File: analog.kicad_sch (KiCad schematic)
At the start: 18 parts, among them Q1 S8550, U2 HX711

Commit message: rough blocking out the pcb
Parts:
- removed C9: 100nF, Capacitor_SMD:C_0603_1608Metric, symbol karl-marel-atomics:KC0603_100nF
- removed JP2: Jumper_2_Open, TestPoint:TestPoint_2Pads_Pitch2.54mm_Drill0.8mm, symbol Jumper:Jumper_2_Open
- removed R11, R12: 100R, Resistor_SMD:R_0603_1608Metric, symbol karl-marel-atomics:KR0603_100R
- added C9: 33pF, Capacitor_SMD:C_0603_1608Metric, symbol karl-marel-atomics:KC0603_33pF
- added R11: 10k, Resistor_SMD:R_0603_1608Metric, symbol karl-marel-atomics:KR0603_10k
- added R12: 0R, Resistor_SMD:R_0603_1608Metric, symbol karl-marel-atomics:KR0603_0R
- added TP1: TestPoint, TestPoint:TestPoint_THTPad_1.5x1.5mm_Drill0.7mm, symbol Connector:TestPoint
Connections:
- net EXC+: now also TP1.1
- net GNDA: now also C3.2, C4.2, R12.1
- net DCLK: now reaches U2.11 (PD_SCK)
- net DOUT: now reaches U2.12 (DOUT)
- net at U2.14 (XI): now also C9.1, R12.2
- net at U2.15 (RATE): now also R11.1
- net REFIN1AA+: no longer names the net of U2.10 (INB+)
- net REFIN1AA-: no longer names the net of U2.9 (INB-)
- new net D_RATE: R11.2
- new net EXT_CLK_IN: C9.2
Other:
- note added: "FIXME: offer channel B?"
- note added: "HX711 can't do a damn thing with 6 wire sensors"
- note added: "TI says R normally not needed, and C should be C0G or film, not x7r!"
- note added: "To use a fixed Ext clock depop R12 and supply on external"
- note removed: "testpads: vhappy ?"
- note removed: "xi to ground means internal. provide option to clock out a "known" rate?"
- moved on the sheet: C3, C4

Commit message: better parts, start pushing layout blocks
SMA is dumb, way too big
the swpa3030 was... unnecessarily small. we're trying to be super chill
power here, don't push it hot.  (Still, 1A was.. really, more than
enough? but 1A is a 40C rise, so.. let's just have less....)
use more caps too. why the fuck not. more filtering, more happy.

holy fuck though, kicad on wayland is giving me the shits!
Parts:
- C3, C4, C9, R10, R11, R12, R13, R15, R8, R9: jlcbasic (none) -> basic
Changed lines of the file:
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@@
+			)
+		)
+		(property "jlcbasic" "basic"
+			(at 123.19 93.98 0)
+			(effects
+				(font
+					(size 1.27 1.27)
+				)
+				(hide yes)
 			)
 		)
@@
 			)
 		)
+		(property "jlcbasic" "basic"
+			(at 209.55 106.68 90)
+			(effects
+				(font
+					(size 1.27 1.27)
+				)
+				(hide yes)
+			)
+		)
 		(pin "1"
 		)
@@
 			)
 		)
+		(property "jlcbasic" "basic"
+			(at 128.27 80.01 0)
+			(effects
+				(font
+					(size 1.27 1.27)
+				)
+				(hide yes)
+			)
+		)
 		(pin "2"
 		)
@@
 			)
 		)
+		(property "jlcbasic" "basic"
+			(at 166.37 73.66 90)
+			(effects
+				(font
+					(size 1.27 1.27)
+				)
+				(hide yes)
+			)
+		)
 		(pin "2"
 		)
@@
 			)
 		)
+		(property "jlcbasic" "basic"
+			(at 228.6 102.87 0)
+			(effects
+				(font
+					(size 1.27 1.27)
+				)
+				(hide yes)
+			)
+		)
 		(pin "2"
 		)
@@
 			)
 		)
+		(property "jlcbasic" "basic"
+			(at 133.35 93.98 0)
+			(effects
+				(font
+					(size 1.27 1.27)
+				)
+				(hide yes)
+			)
+		)
 		(pin "1"
 		)
@@
 		)
 		(property "LCSC Part #" "C25804"
+			(at 151.13 91.44 0)
+			(effects
+				(font
+					(size 1.27 1.27)
+				)
+				(hide yes)
+			)
+		)
+		(property "jlcbasic" "basic"
 			(at 151.13 91.44 0)
 			(effects
@@
 			)
 		)
+		(property "jlcbasic" "basic"
+			(at 240.03 99.06 90)
+			(effects
+				(font
+					(size 1.27 1.27)
+				)
+				(hide yes)
+			)
+		)
 		(pin "2"
 		)
@@
 			)
 		)
+		(property "jlcbasic" "basic"
+			(at 143.51 99.06 0)
+			(effects
+				(font
+					(size 1.27 1.27)
+				)
+				(hide yes)
+			)
+		)
 		(pin "2"
 		)
@@
 			(effects
 				(font
+					(size 1.27 1.27)
+				)
+				(hide yes)
+			)
+		)
+		(property "jlcbasic" "basic"
+			(at 166.37 83.82 90)
+			(effects
+				(font

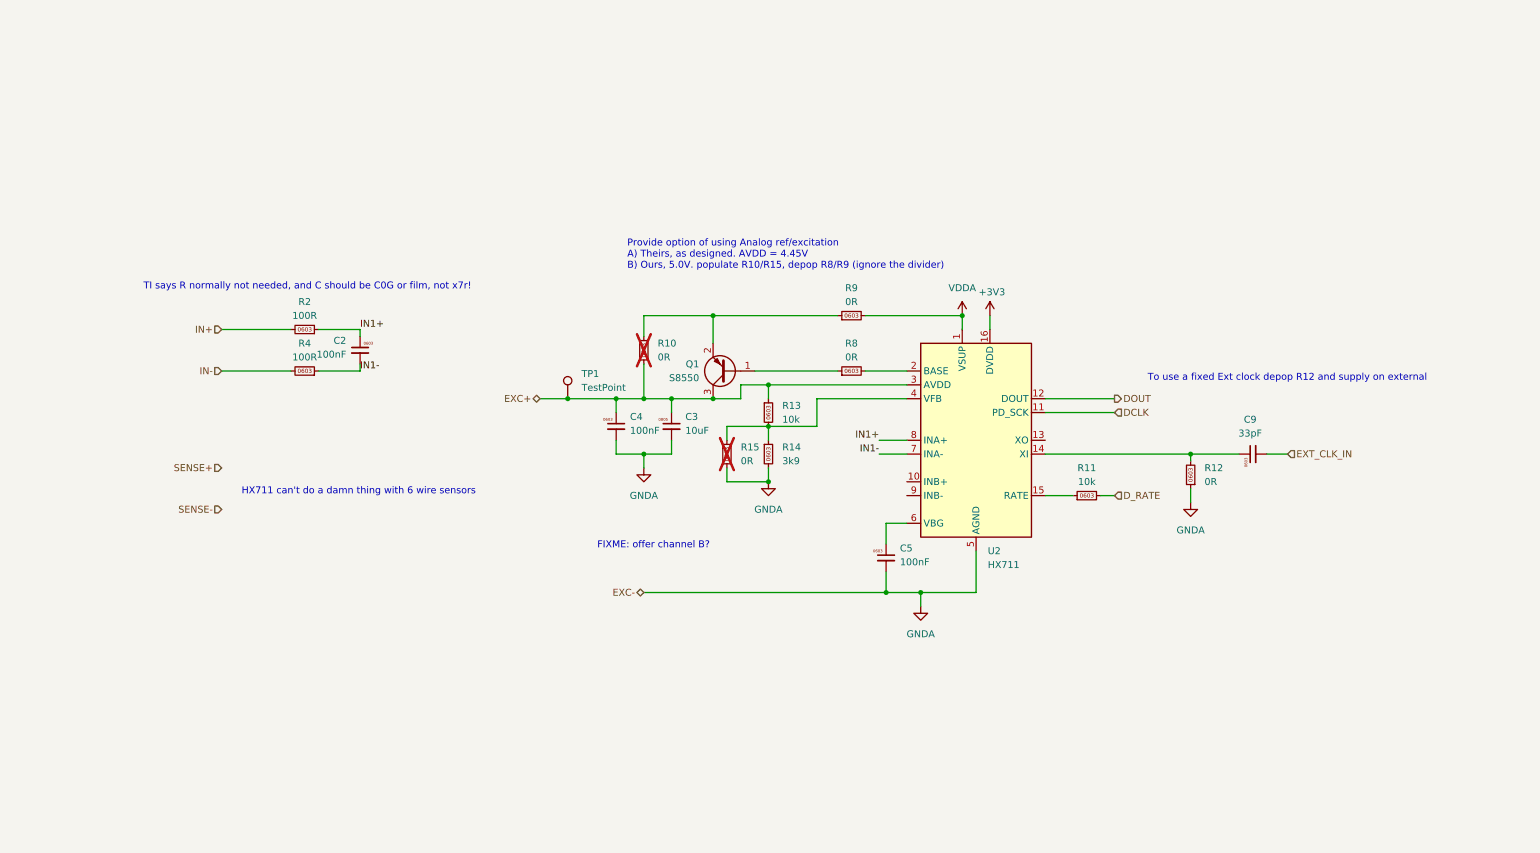
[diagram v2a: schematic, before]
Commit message: add second channel input
switch to vertical connectors, so no concerns abotu edge space.
Allows offering the second channel, even though it's probably useless,
but it sets us up with a style we might be ok with for subsequent
boards.
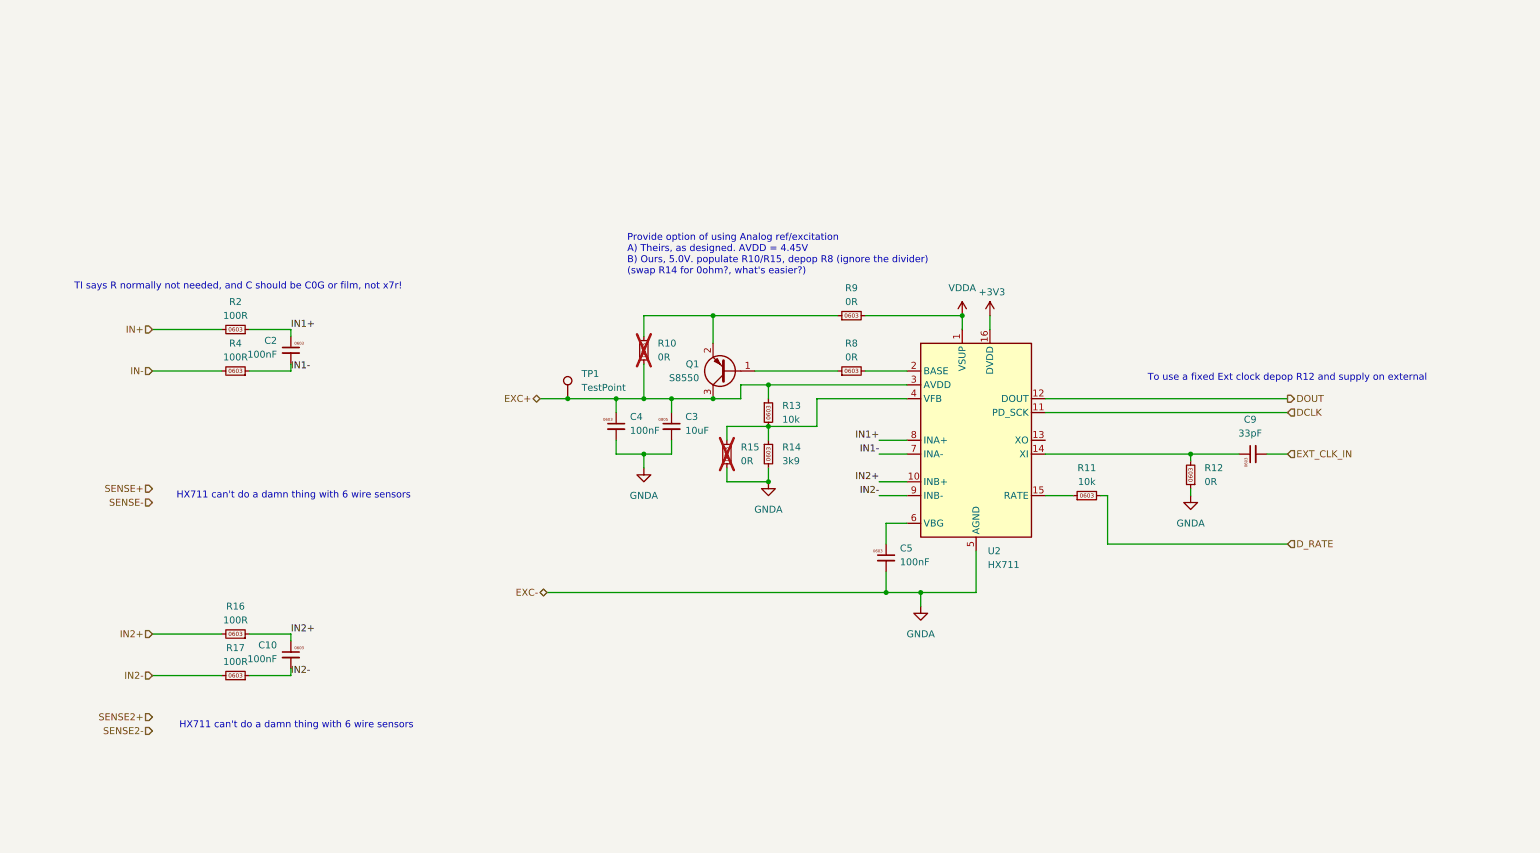
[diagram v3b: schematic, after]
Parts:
- added C10: 100nF, Capacitor_SMD:C_0603_1608Metric, symbol karl-marel-atomics:KC0603_100nF
- added R16, R17: 100R, Resistor_SMD:R_0603_1608Metric, symbol karl-marel-atomics:KR0603_100R
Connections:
- net IN2+: now reaches U2.10 (INB+)
- net IN2+: now also C10.1, R16.1, R16.2
- net IN2-: now reaches U2.9 (INB-)
- net IN2-: now also C10.2, R17.1, R17.2
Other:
- note added: "Provide option of using Analog ref/excitation A) Theirs, as designed. AVDD = 4.45V B) Ours, 5.0V. populate R10/R15, depop R8 (ignore the divider) (swap R14 for 0ohm?, what's easier?)"
- note removed: "FIXME: offer channel B?"
- note removed: "Provide option of using Analog ref/excitation A) Theirs, as designed. AVDD = 4.45V B) Ours, 5.0V. populate R10/R15, depop R8/R9 (ignore the divider)"
- moved on the sheet: C2, R2, R4

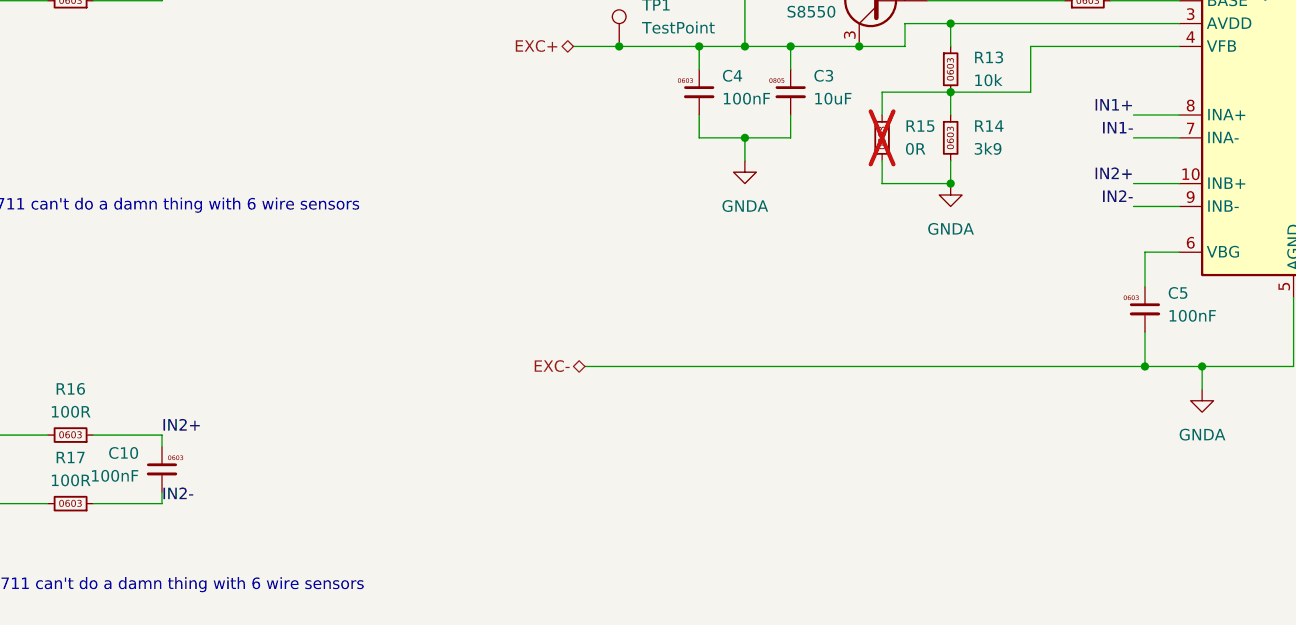
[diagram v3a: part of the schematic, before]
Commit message: chunk out routing
looks okish?

switched x2son for plain sot235, it's better stocked at jlc anyway, and
easier to probe and work with.
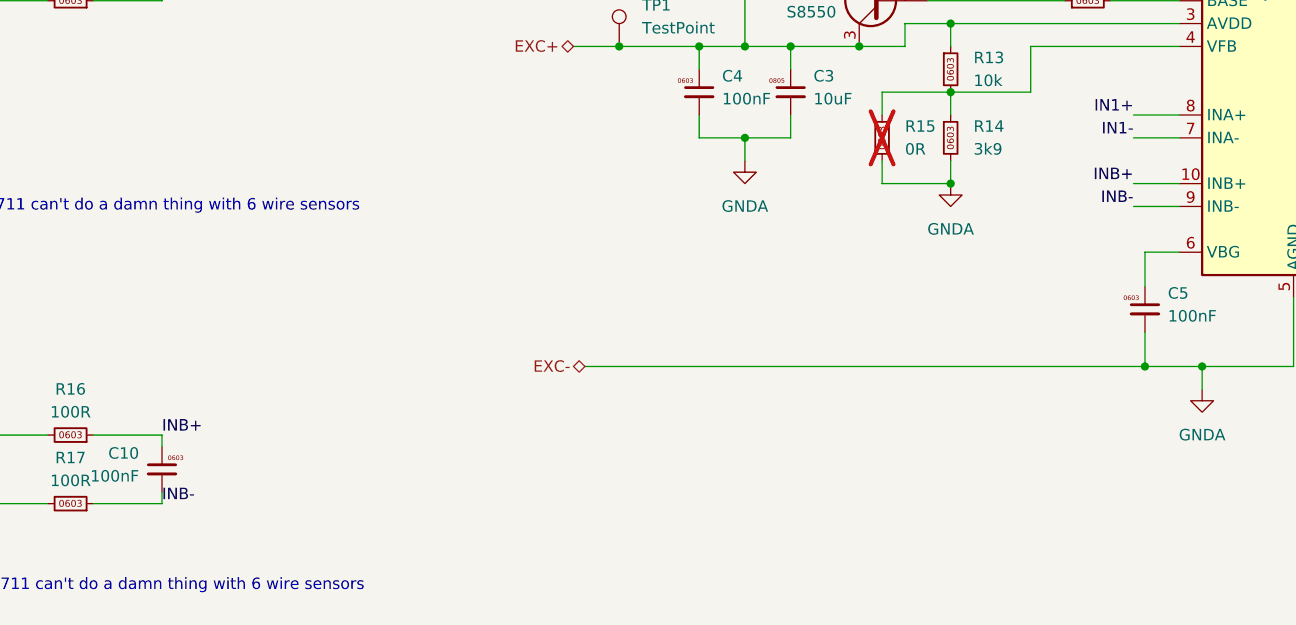
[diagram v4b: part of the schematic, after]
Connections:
- net IN2+: no longer C10.1, R16.1, U2.10 (INB+)
- net IN2-: no longer C10.2, R17.1, U2.9 (INB-)
- new net INB+: C10.1, R16.1, U2.10 (INB+)
- new net INB-: C10.2, R17.1, U2.9 (INB-)
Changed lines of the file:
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@@
 		)
 	)
-	(label "IN2-"
+	(label "INB-"
 		(at 171.45 106.68 180)
 		(effects
@@
 		)
 	)
-	(label "IN2+"
+	(label "INB+"
 		(at 63.5 132.08 0)
 		(effects
@@
 		)
 	)
-	(label "IN2-"
+	(label "INB-"
 		(at 63.5 139.7 0)
 		(effects
@@
 		)
 	)
-	(label "IN2+"
+	(label "INB+"
 		(at 171.45 104.14 180)
 		(effects
